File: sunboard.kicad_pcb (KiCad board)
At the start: 2 copper layers, 24 parts, among them J1 Barrel_Jack_MountingPin, J2 Conn_01x02, Q1 IRLB8721PBF, SW1 SW_Push, U1 STM32F030C8Tx, U4 MIC5209, Y1 Crystal_Small

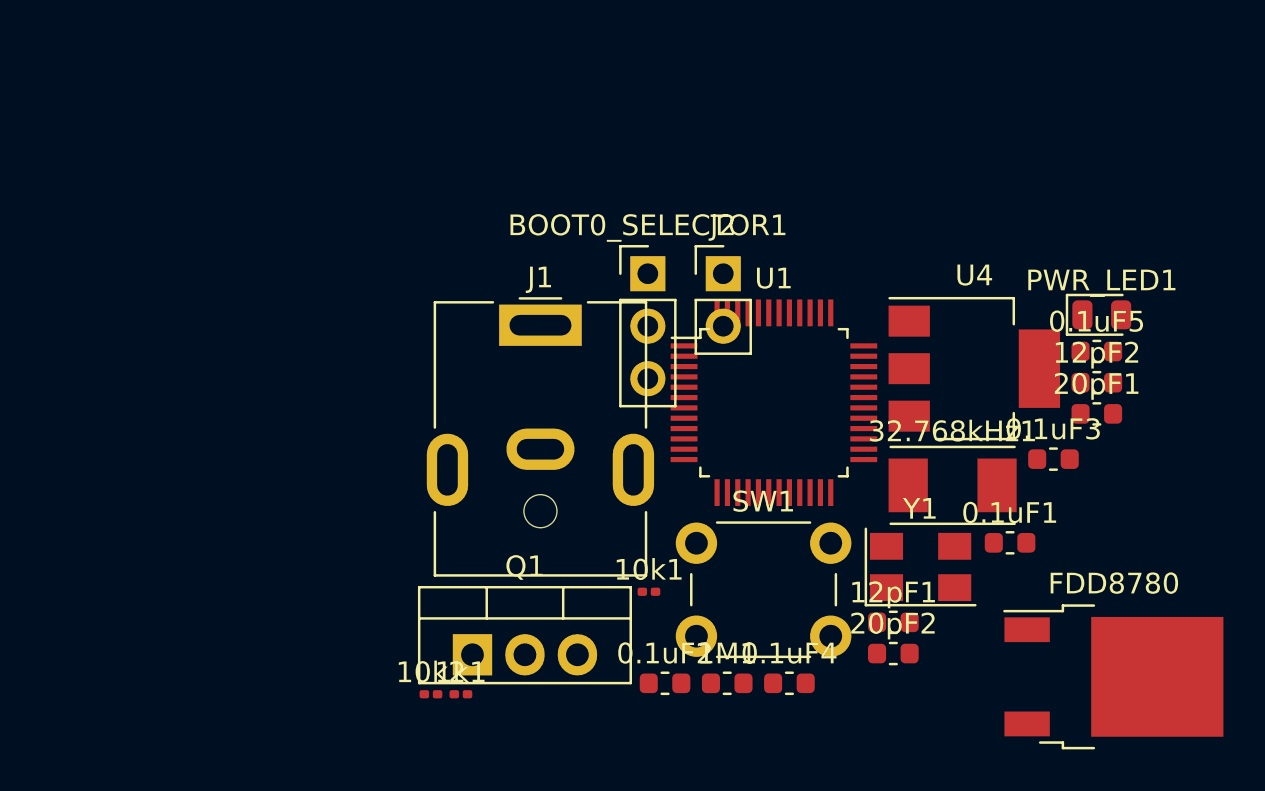
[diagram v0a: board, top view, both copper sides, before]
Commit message: fixed footprints
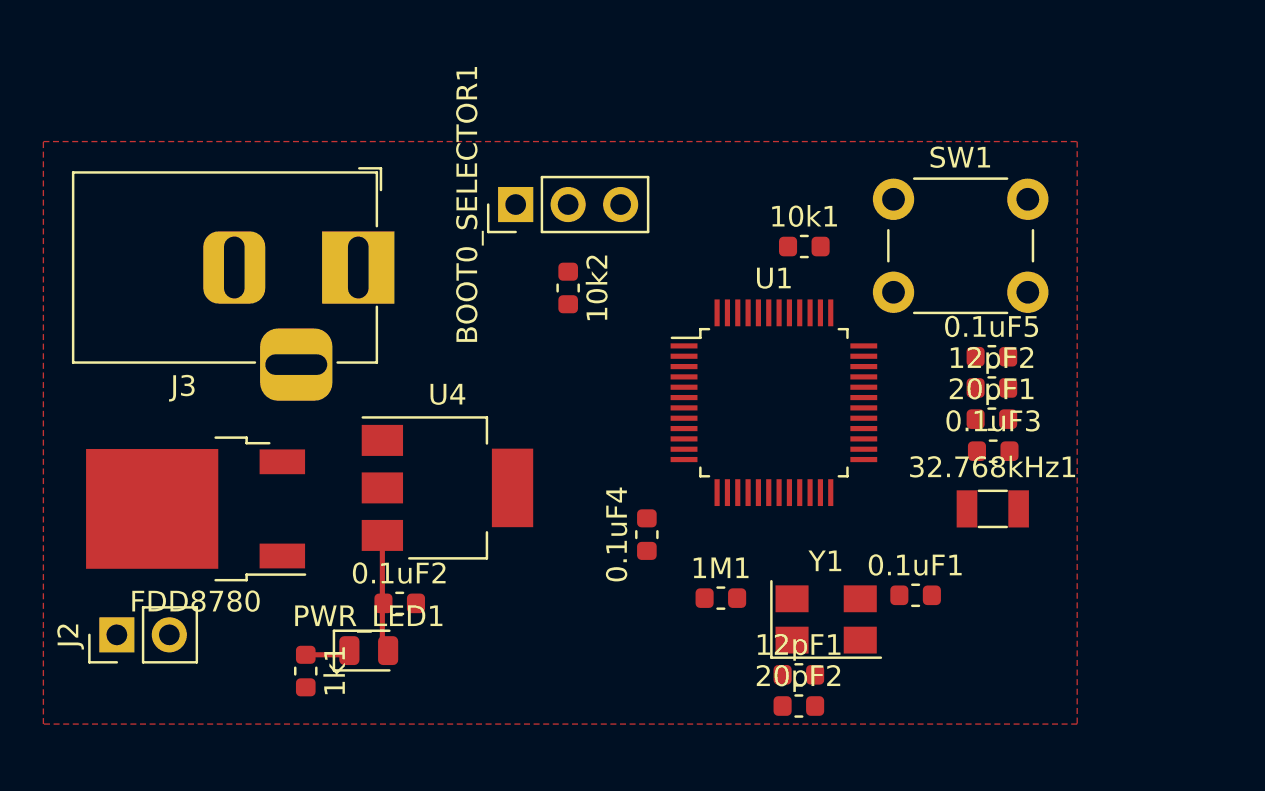
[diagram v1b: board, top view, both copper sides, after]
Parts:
- removed J1: Barrel_Jack_MountingPin, Connector_BarrelJack:BarrelJack_CUI_PJ-063AH_Horizontal
- removed Q1: IRLB8721PBF, Package_TO_SOT_THT:TO-220-3_Vertical
- added J3: Barrel_Jack, Connector_BarrelJack:BarrelJack_Horizontal, F.Cu at (56.6, 31.5)
- 10k1, 10k2, 1k1: footprint Resistor_SMD:R_0201_0603Metric -> Resistor_SMD:R_0603_1608Metric
- 32.768kHz1: footprint Crystal:Crystal_SMD_Abracon_ABM7-2Pin_6.0x3.5mm -> Crystal:Crystal_SMD_3215-2Pin_3.2x1.5mm
- moved FDD8780 45.2 mm to (48.8, 43.2), turned to 180 degrees
- moved PWR_LED1 39.0 mm to (57.1, 50.0)
- moved J2 34.2 mm to (45.0, 49.3), turned to 90 degrees
- moved U4 26.1 mm to (61.0, 42.2)
- moved 10k2 20.8 mm to (66.8, 32.5), turned to 270 degrees
- moved SW1 19.2 mm to (82.5, 28.2)
- moved 10k1 18.3 mm to (78.2, 30.5)
- moved 0.1uF2 13.4 mm to (58.6, 47.8)
- moved 0.1uF4 9.97 mm to (70.6, 44.4), turned to 90 degrees
- moved 1k1 7.59 mm to (54.1, 51.0), turned to 270 degrees
- moved BOOT0_SELECTOR1 7.22 mm to (64.3, 28.4), turned to 90 degrees
- moved Y1 5.23 mm to (79.3, 48.5)
- moved 0.1uF1 5.23 mm to (83.6, 47.4)
- moved 12pF1 5.23 mm to (78.0, 51.2)
- moved 20pF2 5.23 mm to (78.0, 52.7)
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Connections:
- Y1 pad 2: Net-(1M1-Pad2) -> GND
- Y1 pad 3: (no net) -> Net-(1M1-Pad2)
- Y1 pad 4: (no net) -> GND
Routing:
- net +3V3: track 0.00 -> 5.69 mm
- net Net-(1k1-Pad1): track 0.00 -> 2.19 mm
- added copper zone on F.Cu, net GND

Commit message: some placement
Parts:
- 0.1uF1: footprint Capacitor_SMD:C_0603_1608Metric -> Capacitor_SMD:C_0805_2012Metric
- moved 12pF2 26.9 mm to (61.0, 31.8), turned to 90 degrees
- moved 0.1uF1 26.1 mm to (58.9, 38.9)
- moved 32.768kHz1 25.5 mm to (64.3, 32.3)
- moved 20pF2 24.7 mm to (59.7, 36.1), turned to 90 degrees
- moved SW1 24.4 mm to (72.6, 50.5), turned to 180 degrees
- moved 0.1uF5 22.2 mm to (66.3, 42.9), turned to 180 degrees
- moved 12pF1 21.5 mm to (67.8, 32.3), turned to 90 degrees
- moved Y1 20.1 mm to (63.8, 35.8), turned to 180 degrees
- moved 20pF1 19.7 mm to (67.8, 36.1), turned to 270 degrees
- moved 0.1uF3 17.5 mm to (71.9, 32.3), turned to 90 degrees
- moved 1M1 13.5 mm to (63.8, 38.9), turned to 180 degrees
- moved 10k2 7.05 mm to (72.4, 28.2), turned to 90 degrees
- moved J2 3.21 mm to (48.0, 50.3), turned to 270 degrees
- moved PWR_LED1 3.05 mm to (54.1, 50.0), turned to 270 degrees
- moved 1k1 2.74 mm to (51.6, 50.0)
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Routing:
- net +3V3: track 5.69 -> 0.00 mm
- net Net-(1k1-Pad1): track 2.19 -> 0.00 mm
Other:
- board outline added: 42.7 x 27.4 mm
- board text added: "Sunboard Controller v1 Feb 2019"

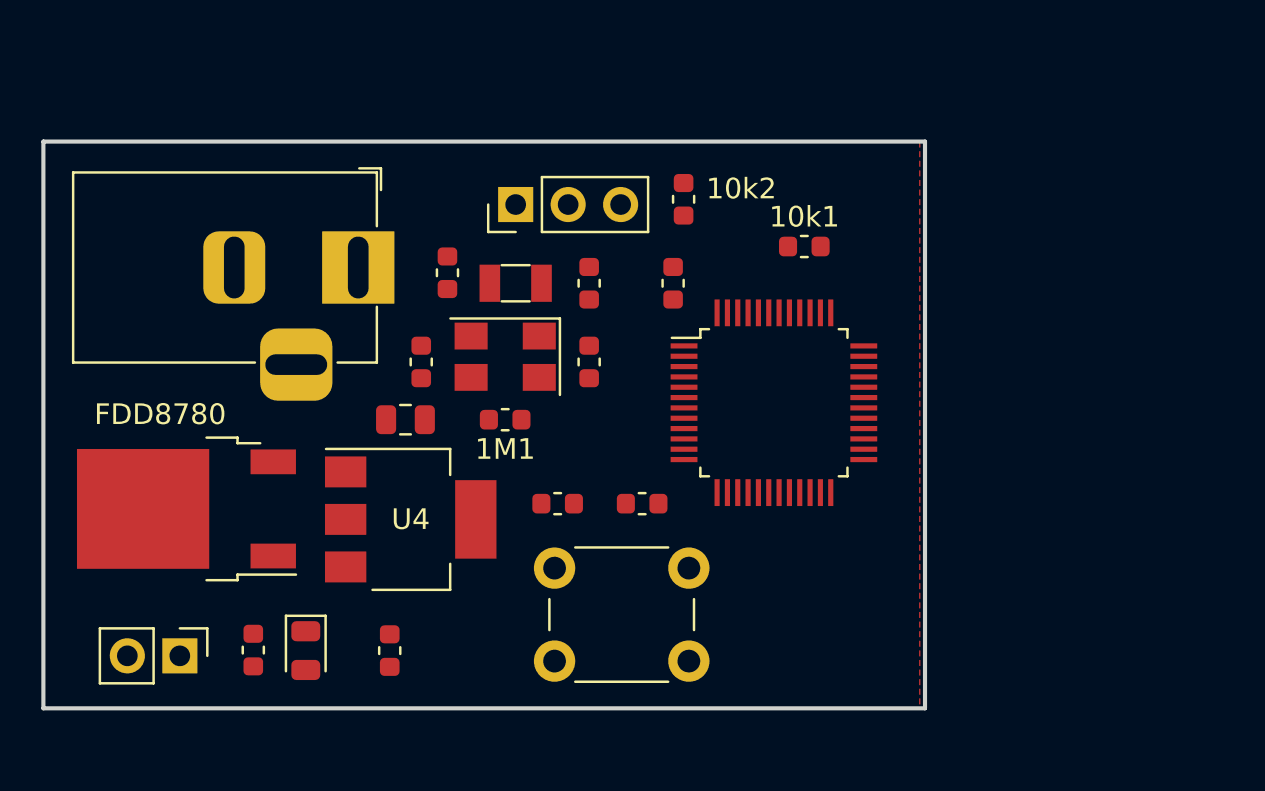
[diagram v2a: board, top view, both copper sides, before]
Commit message: routed everything and added programming headers
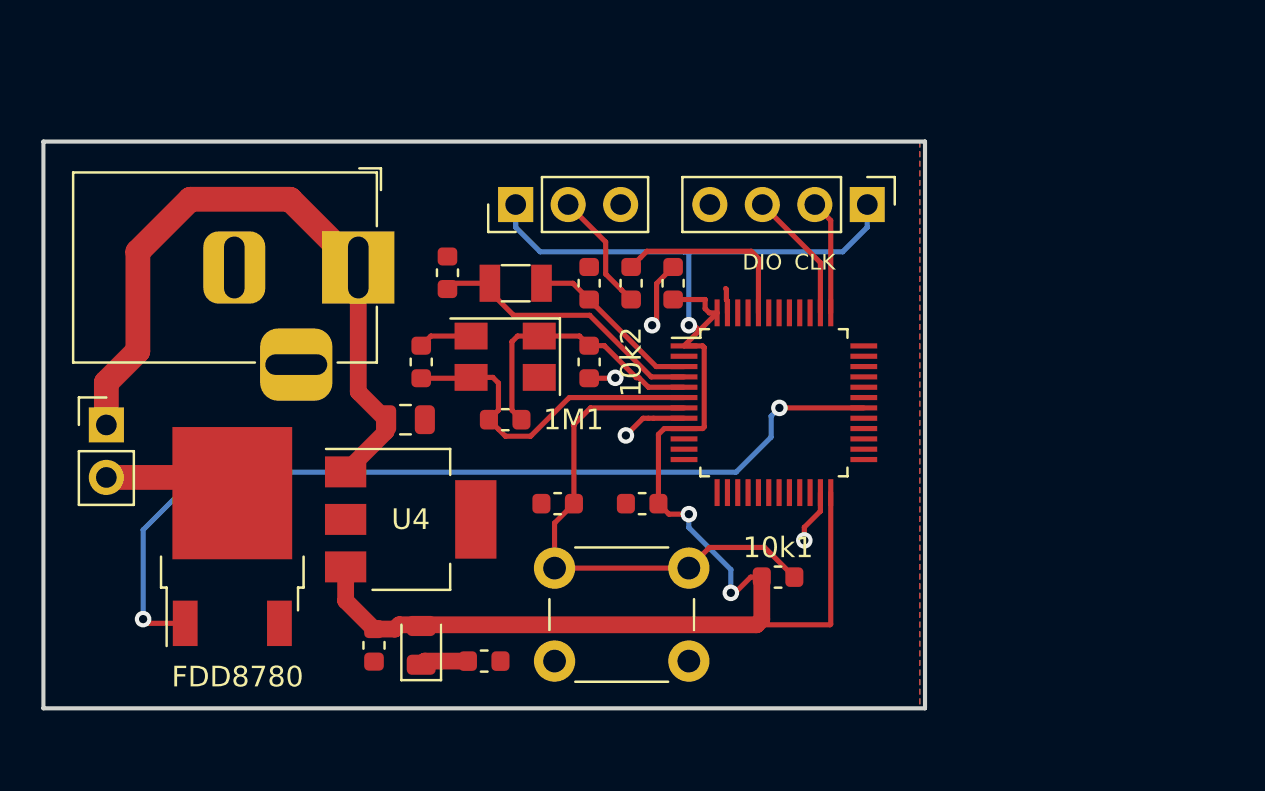
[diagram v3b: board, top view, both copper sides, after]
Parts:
- added J1: Conn_01x04, Connector_PinHeader_2.54mm:PinHeader_1x04_P2.54mm_Vertical, F.Cu at (81.3, 28.4)
- moved 10k1 16.1 mm to (77.0, 46.5)
- moved J2 11.7 mm to (44.5, 39.1), turned to 0 degrees
- moved 1k1 11.2 mm to (62.7, 50.5), turned to 0 degrees
- moved PWR_LED1 5.59 mm to (59.7, 49.8), turned to 90 degrees
- moved 10k2 4.79 mm to (69.8, 32.3)
- moved FDD8780 2.59 mm to (50.5, 44.5), turned to 90 degrees
- moved 0.1uF2 0.80 mm to (57.4, 49.8)
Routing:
- net +3V3: track 0.00 -> 82.8 mm, vias 0 -> 3
- net /PWM: track 0.00 -> 44.4 mm, vias 0 -> 2
- net +12V: track 0.00 -> 33.4 mm
- net /RESET: track 0.00 -> 25.6 mm
- net Net-(1M1-Pad2): track 0.00 -> 16.4 mm
- net GND: track 0.00 -> 14.1 mm, vias 0 -> 4
- net Net-(12pF2-Pad1): track 0.00 -> 13.7 mm
- net Net-(1M1-Pad1): track 0.00 -> 13.4 mm
- net /BOOT0: track 0.00 -> 9.26 mm
- net Net-(12pF1-Pad1): track 0.00 -> 8.57 mm
- net /LED_GND: track 0.00 -> 6.41 mm
- net /SWDIO: track 0.00 -> 6.41 mm
- net Net-(10k2-Pad1): track 0.00 -> 5.86 mm
- net /SWCLK: track 0.00 -> 5.56 mm
- net Net-(1k1-Pad1): track 0.00 -> 2.33 mm
- added copper zone on B.Cu, net GND
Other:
- board text added: "CLK"
- board text added: "DIO"

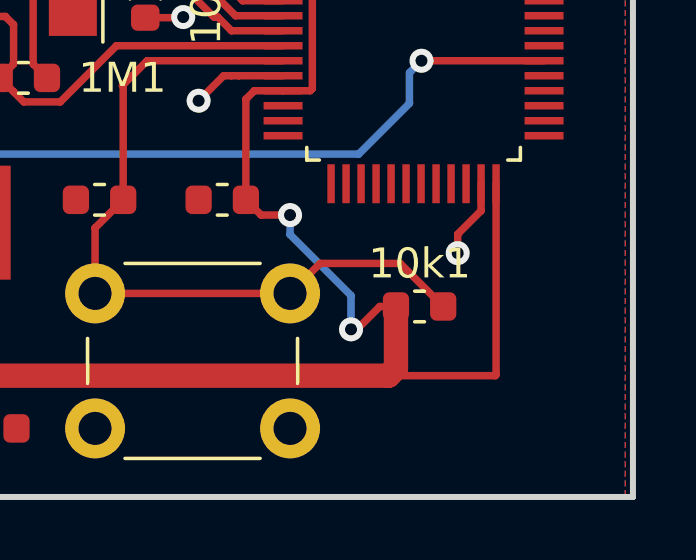
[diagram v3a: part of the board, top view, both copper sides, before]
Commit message: added extra header for two GPIOs
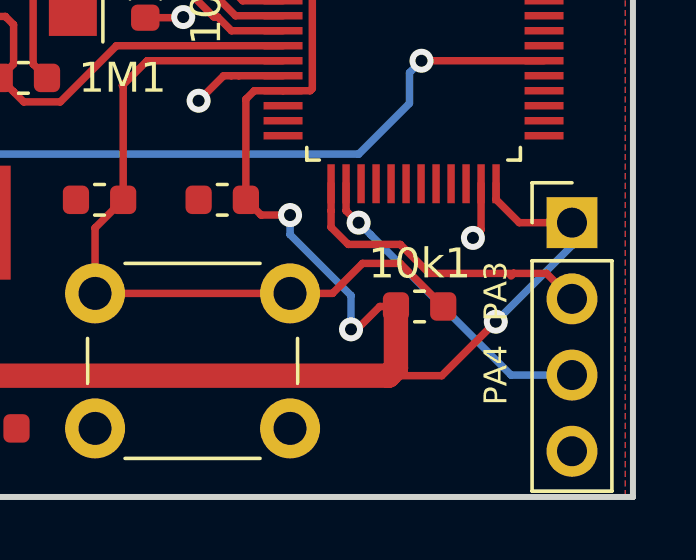
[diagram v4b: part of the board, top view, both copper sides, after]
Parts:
- added J4: Conn_01x04, Connector_PinHeader_2.54mm:PinHeader_1x04_P2.54mm_Vertical, F.Cu at (82.0, 43.7)
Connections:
- U1 pad 13: Net-(U1-Pad13) -> /PA3
- U1 pad 14: Net-(U1-Pad14) -> /PA4
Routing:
- net /PA4: track 0.00 -> 10.7 mm, vias 0 -> 1
- net /PA3: track 0.00 -> 10.6 mm
- net +3V3: track 82.8 -> 84.9 mm, vias 3 -> 4
- net GND: track 14.1 -> 13.4 mm
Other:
- board text added: "PA3"
- board text added: "PA4"
